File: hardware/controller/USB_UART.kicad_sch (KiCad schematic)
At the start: 7 parts, among them IC701 CP2102N-A02-GQFN28

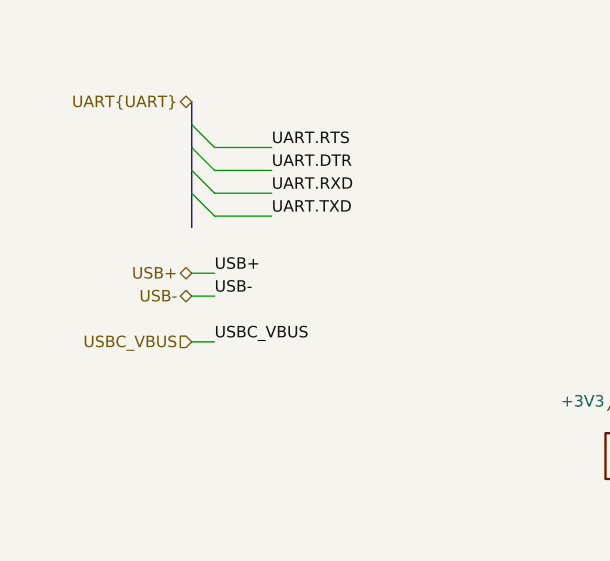
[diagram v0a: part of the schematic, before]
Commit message: fixed 3d models. rounded edges of pcb
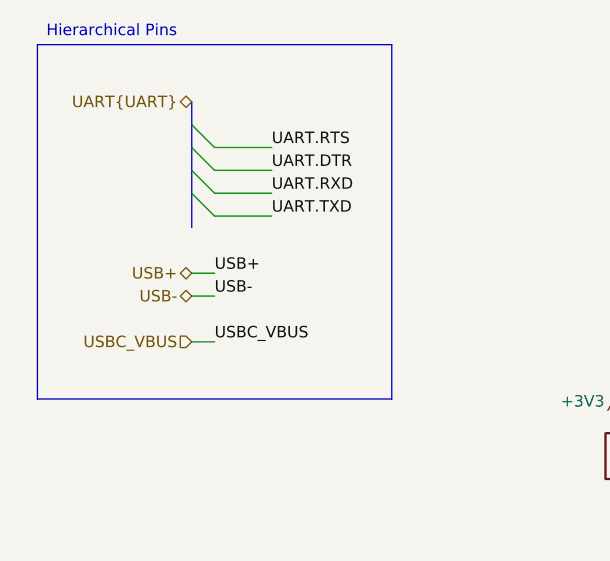
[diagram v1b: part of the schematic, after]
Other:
- note added: "Hierarchical Pins"
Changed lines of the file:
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@@
 		(members "RTS" "DTR" "RXD" "TXD")
+	)
+	(rectangle
+		(start 19.685 34.29)
+		(end 59.055 73.66)
+		(stroke
+			(width 0)
+			(type default)
+		)
+		(fill
+			(type none)
+		)
 	)
 	(text "Note: this is not actually necessary for ESP32-S3\nsince it has native USB support\n\nI am including it anyways just for fun"
@@
 		(effects
 			(font
+				(size 1.27 1.27)
+			)
+		)
+	)
+	(text "Hierarchical Pins"
+		(exclude_from_sim no)
+		(at 27.94 32.893 0)
+		(effects
+			(font

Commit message: a
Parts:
- R704: footprint SamacSys_Parts:RESC2012X60N -> RESC2012X60N
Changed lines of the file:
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@@
 			)
 		)
-		(property "Footprint" "SamacSys_Parts:RESC2012X60N"
+		(property "Footprint" "RESC2012X60N"
 			(at 109.22 30.81 0)
 			(effects
@@
 			)
 		)
-		(property "Datasheet" "~"
+		(property "Datasheet" "https://componentsearchengine.com/Datasheets/2/ASC0805-10KFT5.pdf"
 			(at 109.22 -69.19 0)
 			(effects
@@
 			)
 		)
-		(property "Description" "Resistor"
+		(property "Description" "WELWYN - ASC0805-10KFT5 - RESISTOR, ANTI SULPHUR, 10K, 0.125W, 1%"
 			(at 123.19 127 0)
 			(effects

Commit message: save before nuke
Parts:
- R120: renamed from R704; footprint RESC2012X60N -> SamacSys_Parts:RESC2012X60N
- renumbered C701 to C117, C702 to C118, IC701 to IC102, R701 to R117, R702 to R118, R703 to R119
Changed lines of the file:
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@@
 		(on_board yes)
 		(dnp no)
-		(property "Reference" "R704"
+		(property "Reference" "R120"
 			(at 116.84 125.73 0)
 			(effects
@@
 			)
 		)
-		(property "Footprint" "RESC2012X60N"
+		(property "Footprint" "SamacSys_Parts:RESC2012X60N"
 			(at 109.22 30.81 0)
 			(effects
@@
 			(project "controller"
 				(path "/869bea87-c885-4ead-826b-3f34ceacafad/6716075d-3941-4cbb-90c0-6bb554220bff"
-					(reference "R704")
+					(reference "R120")
 					(unit 1)
 				)
@@
 		(on_board yes)
 		(dnp no)
-		(property "Reference" "IC701"
+		(property "Reference" "IC102"
 			(at 124.714 60.706 0)
 			(effects
@@
 			(project ""
 				(path "/869bea87-c885-4ead-826b-3f34ceacafad/6716075d-3941-4cbb-90c0-6bb554220bff"
-					(reference "IC701")
+					(reference "IC102")
 					(unit 1)
 				)
@@
 		(dnp no)
 		(fields_autoplaced yes)
-		(property "Reference" "C702"
+		(property "Reference" "C118"
 			(at 95.25 102.8699 0)
 			(effects
@@
 			(project "controller"
 				(path "/869bea87-c885-4ead-826b-3f34ceacafad/6716075d-3941-4cbb-90c0-6bb554220bff"
-					(reference "C702")
+					(reference "C118")
 					(unit 1)
 				)
@@
 		(on_board yes)
 		(dnp no)
-		(property "Reference" "#PWR0702"
+		(property "Reference" "#PWR0158"
 			(at 85.09 102.87 0)
 			(effects
@@
 			(project ""
 				(path "/869bea87-c885-4ead-826b-3f34ceacafad/6716075d-3941-4cbb-90c0-6bb554220bff"
-					(reference "#PWR0702")
+					(reference "#PWR0158")
 					(unit 1)
 				)
@@
 		(on_board yes)
 		(dnp no)
-		(property "Reference" "R702"
+		(property "Reference" "R118"
 			(at 90.678 124.46 90)
 			(effects
@@
 			(project ""
 				(path "/869bea87-c885-4ead-826b-3f34ceacafad/6716075d-3941-4cbb-90c0-6bb554220bff"
-					(reference "R702")
+					(reference "R118")
 					(unit 1)
 				)
@@
 		(dnp no)
 		(fields_autoplaced yes)
-		(property "Reference" "#PWR0705"
+		(property "Reference" "#PWR0161"
 			(at 123.19 137.16 0)
 			(effects
@@
 			(project "controller"
 				(path "/869bea87-c885-4ead-826b-3f34ceacafad/6716075d-3941-4cbb-90c0-6bb554220bff"
-					(reference "#PWR0705")
+					(reference "#PWR0161")
 					(unit 1)
 				)
@@
 		(dnp no)
 		(fields_autoplaced yes)
-		(property "Reference" "#PWR0703"
+		(property "Reference" "#PWR0159"
 			(at 86.36 116.84 0)
 			(effects
@@
 			(project ""
 				(path "/869bea87-c885-4ead-826b-3f34ceacafad/6716075d-3941-4cbb-90c0-6bb554220bff"
-					(reference "#PWR0703")
+					(reference "#PWR0159")
 					(unit 1)
 				)
@@
 		(dnp no)
 		(fields_autoplaced yes)
-		(property "Reference" "R703"
+		(property "Reference" "R119"
 			(at 100.33 125.7299 0)
 			(effects
@@
 			(project "controller"
 				(path "/869bea87-c885-4ead-826b-3f34ceacafad/6716075d-3941-4cbb-90c0-6bb554220bff"
-					(reference "R703")
+					(reference "R119")
 					(unit 1)
 				)
@@
 		(on_board yes)
 		(dnp no)
-		(property "Reference" "#PWR0701"
+		(property "Reference" "#PWR0157"
 			(at 83.82 80.01 0)
 			(effects
@@
 			(project "controller"
 				(path "/869bea87-c885-4ead-826b-3f34ceacafad/6716075d-3941-4cbb-90c0-6bb554220bff"
-					(reference "#PWR0701")
+					(reference "#PWR0157")
 					(unit 1)
 				)
@@
 		(dnp no)
 		(fields_autoplaced yes)
-		(property "Reference" "#PWR0706"
+		(property "Reference" "#PWR0162"
 			(at 132.08 137.16 0)
 			(effects
@@
 			(project "controller"
 				(path "/869bea87-c885-4ead-826b-3f34ceacafad/6716075d-3941-4cbb-90c0-6bb554220bff"
-					(reference "#PWR0706")
+					(reference "#PWR0162")
 					(unit 1)
 				)
@@
 		(dnp no)
 		(fields_autoplaced yes)
-		(property "Reference" "C701"
+		(property "Reference" "C117"
 			(at 83.82 102.8699 0)
 			(effects
@@
 			(project "controller"
 				(path "/869bea87-c885-4ead-826b-3f34ceacafad/6716075d-3941-4cbb-90c0-6bb554220bff"
-					(reference "C701")
+					(reference "C117")
 					(unit 1)
 				)
@@
 		(on_board yes)
 		(dnp no)
-		(property "Reference" "R701"
+		(property "Reference" "R117"
 			(at 85.09 78.74 0)
 			(effects
@@
 			(project "controller"
 				(path "/869bea87-c885-4ead-826b-3f34ceacafad/6716075d-3941-4cbb-90c0-6bb554220bff"
-					(reference "R701")
+					(reference "R117")
 					(unit 1)
 				)
@@
 		(dnp no)
 		(fields_autoplaced yes)
-		(property "Reference" "#PWR0704"
+		(property "Reference" "#PWR0160"
 			(at 97.79 137.16 0)
 			(effects
@@
 			(project "controller"
 				(path "/869bea87-c885-4ead-826b-3f34ceacafad/6716075d-3941-4cbb-90c0-6bb554220bff"
-					(reference "#PWR0704")
+					(reference "#PWR0160")
 					(unit 1)
 				)

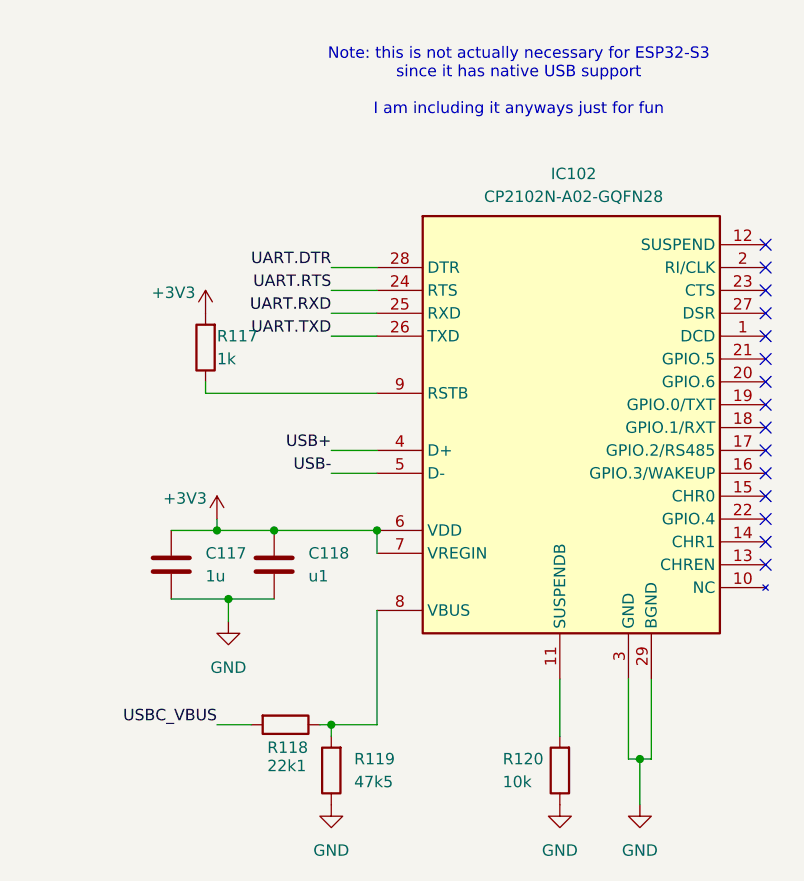
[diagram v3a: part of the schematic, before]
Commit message: clean up DRC. need to add stitching vias and figure out why inner ground plane isnt connected to F.Cu pour
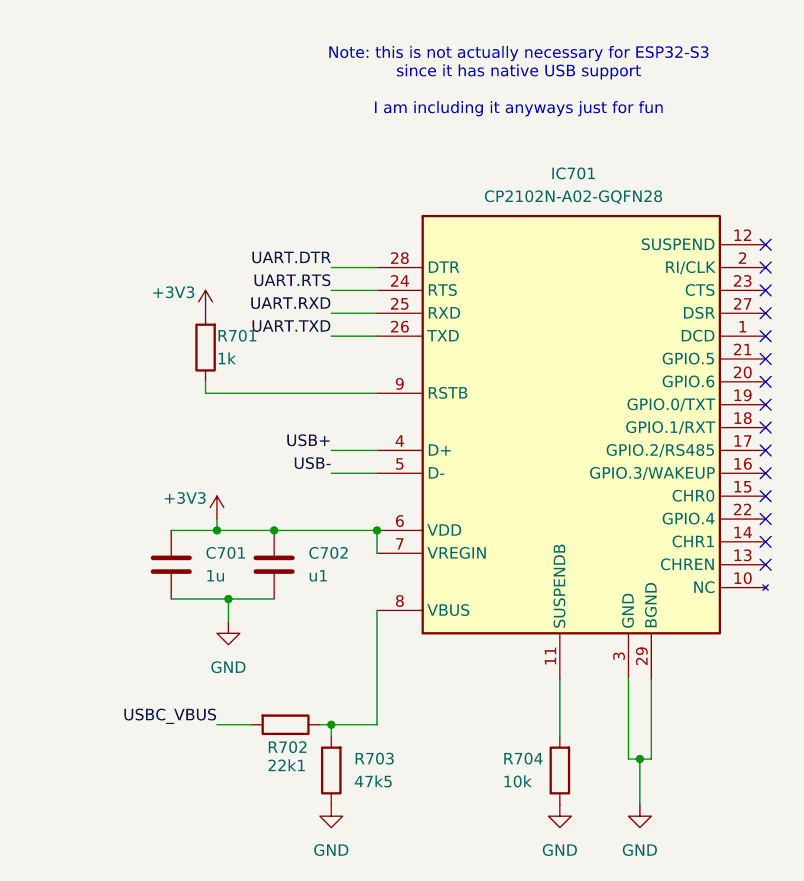
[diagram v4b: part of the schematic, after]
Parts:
- renumbered C117 to C701, C118 to C702, IC102 to IC701, R117 to R701, R118 to R702, R119 to R703, R120 to R704
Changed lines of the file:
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@@
 		(on_board yes)
 		(dnp no)
-		(property "Reference" "R120"
+		(property "Reference" "R704"
 			(at 116.84 125.73 0)
 			(effects
@@
 			(project "controller"
 				(path "/869bea87-c885-4ead-826b-3f34ceacafad/6716075d-3941-4cbb-90c0-6bb554220bff"
-					(reference "R120")
+					(reference "R704")
 					(unit 1)
 				)
@@
 		(on_board yes)
 		(dnp no)
-		(property "Reference" "IC102"
+		(property "Reference" "IC701"
 			(at 124.714 60.706 0)
 			(effects
@@
 			(project ""
 				(path "/869bea87-c885-4ead-826b-3f34ceacafad/6716075d-3941-4cbb-90c0-6bb554220bff"
-					(reference "IC102")
+					(reference "IC701")
 					(unit 1)
 				)
@@
 		(dnp no)
 		(fields_autoplaced yes)
-		(property "Reference" "C118"
+		(property "Reference" "C702"
 			(at 95.25 102.8699 0)
 			(effects
@@
 			(project "controller"
 				(path "/869bea87-c885-4ead-826b-3f34ceacafad/6716075d-3941-4cbb-90c0-6bb554220bff"
-					(reference "C118")
+					(reference "C702")
 					(unit 1)
 				)
@@
 		(on_board yes)
 		(dnp no)
-		(property "Reference" "#PWR0158"
+		(property "Reference" "#PWR0702"
 			(at 85.09 102.87 0)
 			(effects
@@
 			(project ""
 				(path "/869bea87-c885-4ead-826b-3f34ceacafad/6716075d-3941-4cbb-90c0-6bb554220bff"
-					(reference "#PWR0158")
+					(reference "#PWR0702")
 					(unit 1)
 				)
@@
 		(on_board yes)
 		(dnp no)
-		(property "Reference" "R118"
+		(property "Reference" "R702"
 			(at 90.678 124.46 90)
 			(effects
@@
 			(project ""
 				(path "/869bea87-c885-4ead-826b-3f34ceacafad/6716075d-3941-4cbb-90c0-6bb554220bff"
-					(reference "R118")
+					(reference "R702")
 					(unit 1)
 				)
@@
 		(dnp no)
 		(fields_autoplaced yes)
-		(property "Reference" "#PWR0161"
+		(property "Reference" "#PWR0705"
 			(at 123.19 137.16 0)
 			(effects
@@
 			(project "controller"
 				(path "/869bea87-c885-4ead-826b-3f34ceacafad/6716075d-3941-4cbb-90c0-6bb554220bff"
-					(reference "#PWR0161")
+					(reference "#PWR0705")
 					(unit 1)
 				)
@@
 		(dnp no)
 		(fields_autoplaced yes)
-		(property "Reference" "#PWR0159"
+		(property "Reference" "#PWR0703"
 			(at 86.36 116.84 0)
 			(effects
@@
 			(project ""
 				(path "/869bea87-c885-4ead-826b-3f34ceacafad/6716075d-3941-4cbb-90c0-6bb554220bff"
-					(reference "#PWR0159")
+					(reference "#PWR0703")
 					(unit 1)
 				)
@@
 		(dnp no)
 		(fields_autoplaced yes)
-		(property "Reference" "R119"
+		(property "Reference" "R703"
 			(at 100.33 125.7299 0)
 			(effects
@@
 			(project "controller"
 				(path "/869bea87-c885-4ead-826b-3f34ceacafad/6716075d-3941-4cbb-90c0-6bb554220bff"
-					(reference "R119")
+					(reference "R703")
 					(unit 1)
 				)
@@
 		(on_board yes)
 		(dnp no)
-		(property "Reference" "#PWR0157"
+		(property "Reference" "#PWR0701"
 			(at 83.82 80.01 0)
 			(effects
@@
 			(project "controller"
 				(path "/869bea87-c885-4ead-826b-3f34ceacafad/6716075d-3941-4cbb-90c0-6bb554220bff"
-					(reference "#PWR0157")
+					(reference "#PWR0701")
 					(unit 1)
 				)
@@
 		(dnp no)
 		(fields_autoplaced yes)
-		(property "Reference" "#PWR0162"
+		(property "Reference" "#PWR0706"
 			(at 132.08 137.16 0)
 			(effects
@@
 			(project "controller"
 				(path "/869bea87-c885-4ead-826b-3f34ceacafad/6716075d-3941-4cbb-90c0-6bb554220bff"
-					(reference "#PWR0162")
+					(reference "#PWR0706")
 					(unit 1)
 				)
@@
 		(dnp no)
 		(fields_autoplaced yes)
-		(property "Reference" "C117"
+		(property "Reference" "C701"
 			(at 83.82 102.8699 0)
 			(effects
@@
 			(project "controller"
 				(path "/869bea87-c885-4ead-826b-3f34ceacafad/6716075d-3941-4cbb-90c0-6bb554220bff"
-					(reference "C117")
+					(reference "C701")
 					(unit 1)
 				)
@@
 		(on_board yes)
 		(dnp no)
-		(property "Reference" "R117"
+		(property "Reference" "R701"
 			(at 85.09 78.74 0)
 			(effects
@@
 			(project "controller"
 				(path "/869bea87-c885-4ead-826b-3f34ceacafad/6716075d-3941-4cbb-90c0-6bb554220bff"
-					(reference "R117")
+					(reference "R701")
 					(unit 1)
 				)
@@
 		(dnp no)
 		(fields_autoplaced yes)
-		(property "Reference" "#PWR0160"
+		(property "Reference" "#PWR0704"
 			(at 97.79 137.16 0)
 			(effects
@@
 			(project "controller"
 				(path "/869bea87-c885-4ead-826b-3f34ceacafad/6716075d-3941-4cbb-90c0-6bb554220bff"
-					(reference "#PWR0160")
+					(reference "#PWR0704")
 					(unit 1)
 				)

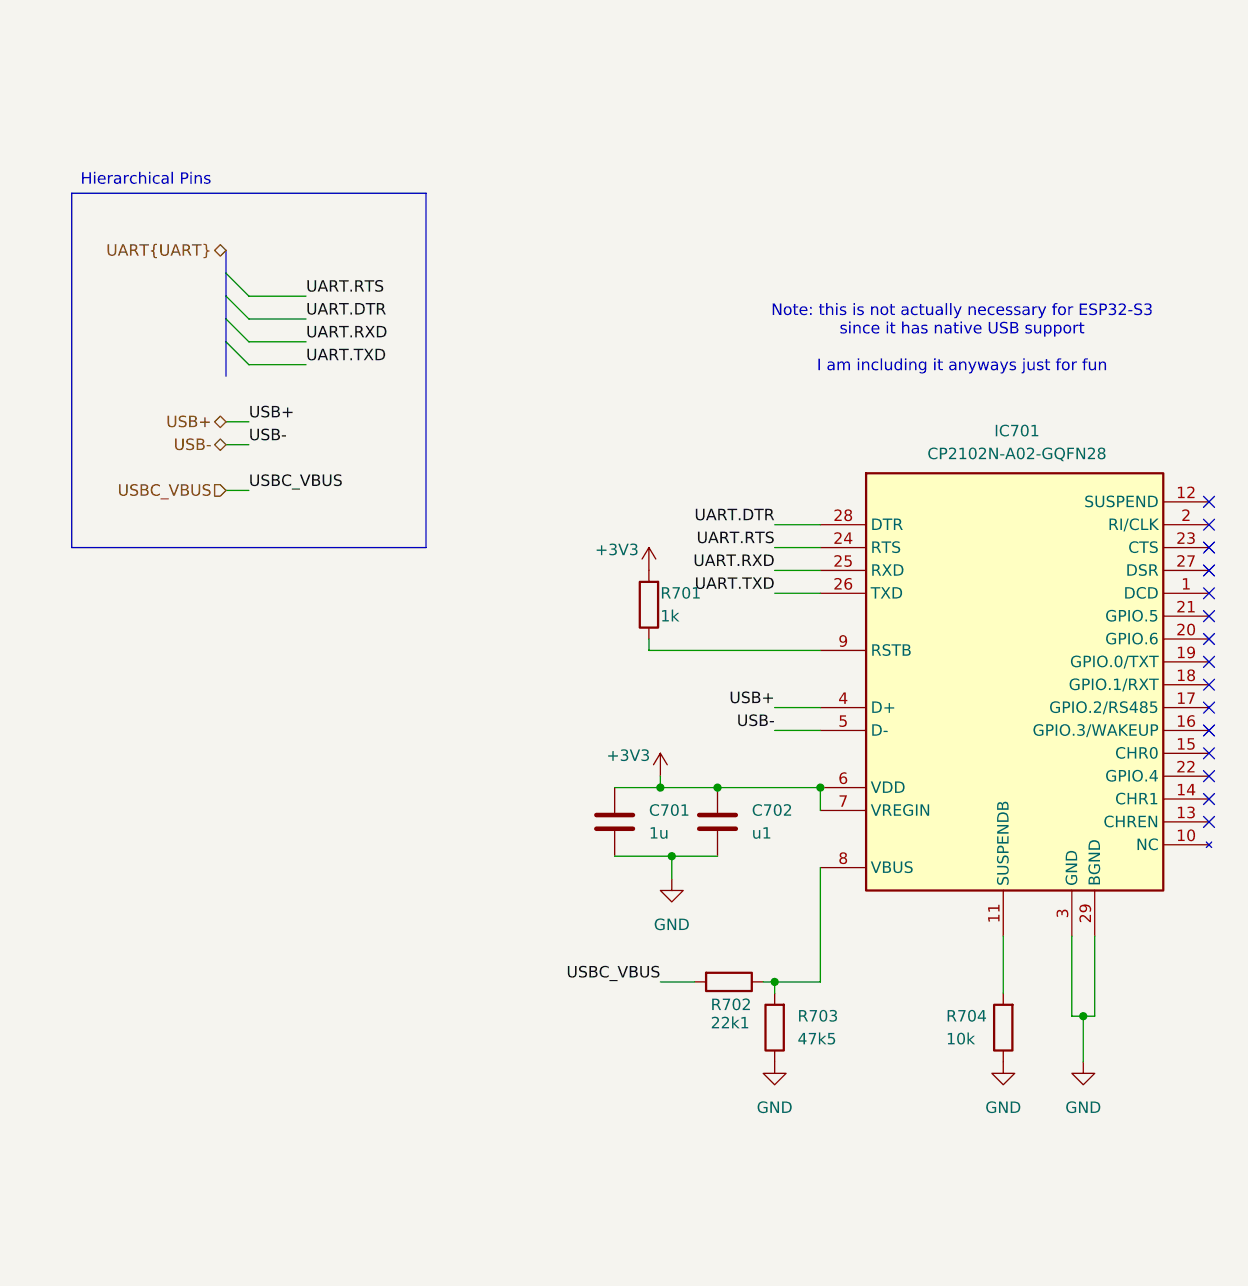
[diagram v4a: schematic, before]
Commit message: save before axing motor driver ic's
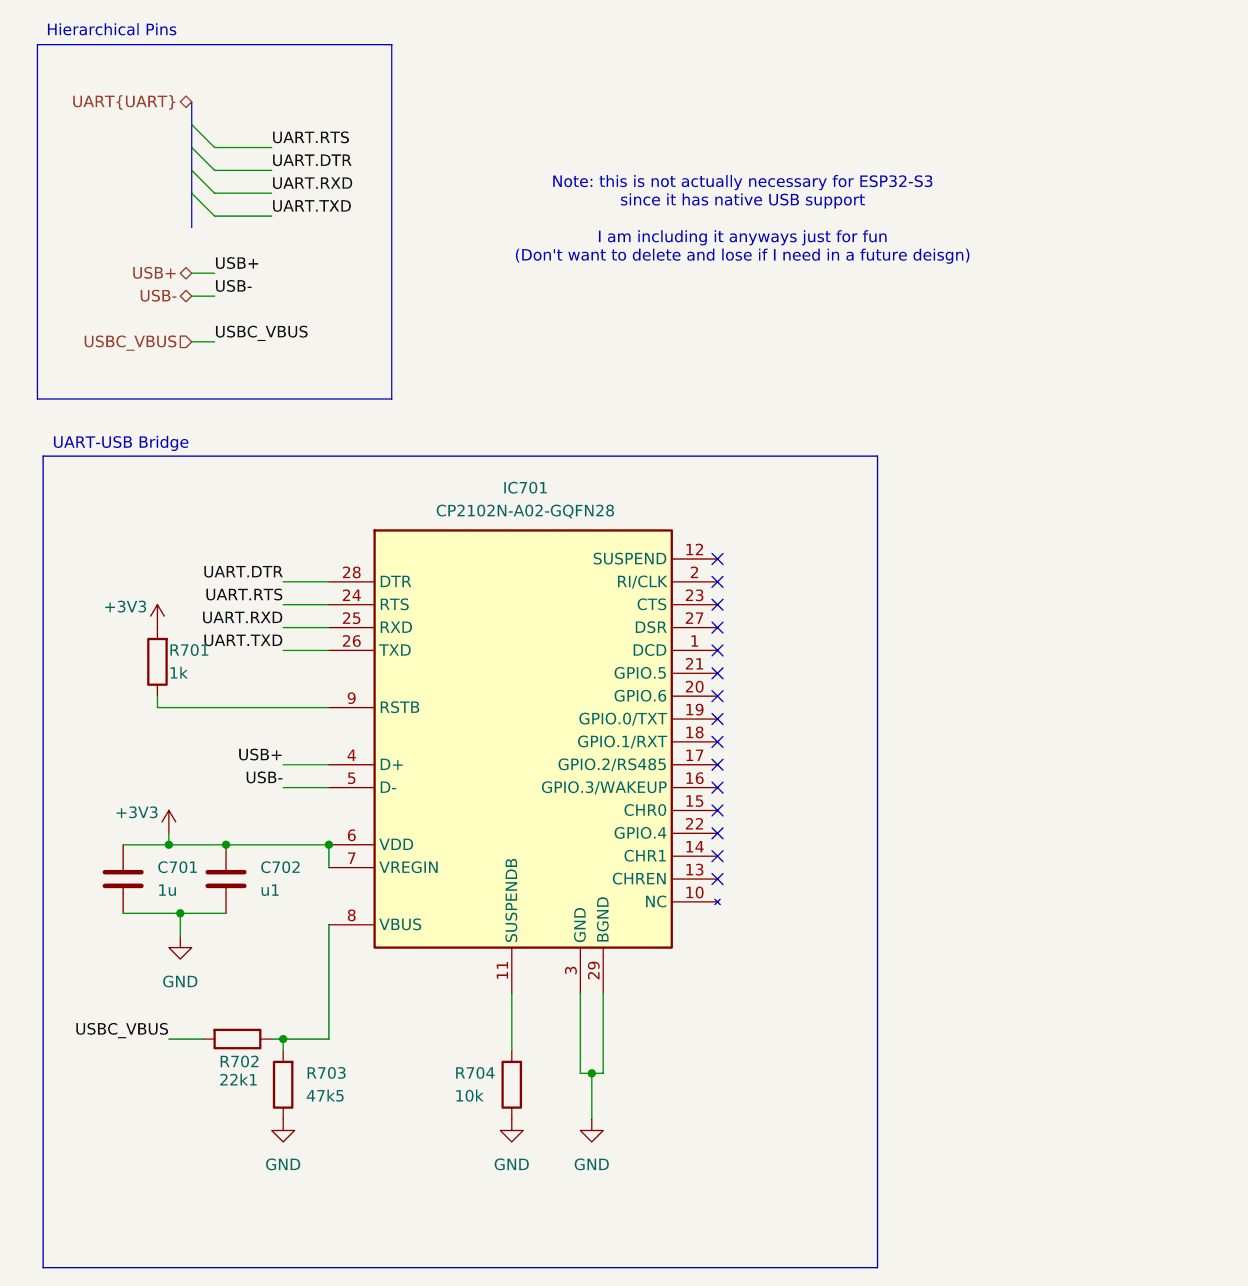
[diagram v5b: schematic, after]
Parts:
- R702: Mouser Price/Stock https://www.mouser.com/ProductDetail/Vishay/CRCW060322K1FKE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 -> https://www.mouser.co.uk/ProductDetail/Vishay/CRCW060322K1F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
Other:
- note added: "Note: this is not actually necessary for ESP32-S3 since it has native USB support I am including it anyways just for fun (Don't want to delete and lose if I need in a future deisgn)"
- note added: "UART-USB Bridge"
- note removed: "Note: this is not actually necessary for ESP32-S3 since it has native USB support I am including it anyways just for fun"
- moved on the sheet: C701, C702, IC701, R701, R702, R703, R704
